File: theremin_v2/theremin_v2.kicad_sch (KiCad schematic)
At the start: 34 parts, among them J2 USB_C_Receptacle_USB2.0, J3 Conn_01x01_Pin, SW1 Reset, SW2 Boot, U1 AD8001AR, U2 HEF4093B, U3 AD8001AR, U4 ESP32-S2-SOLO, U5 LD1117S33TR_SOT223

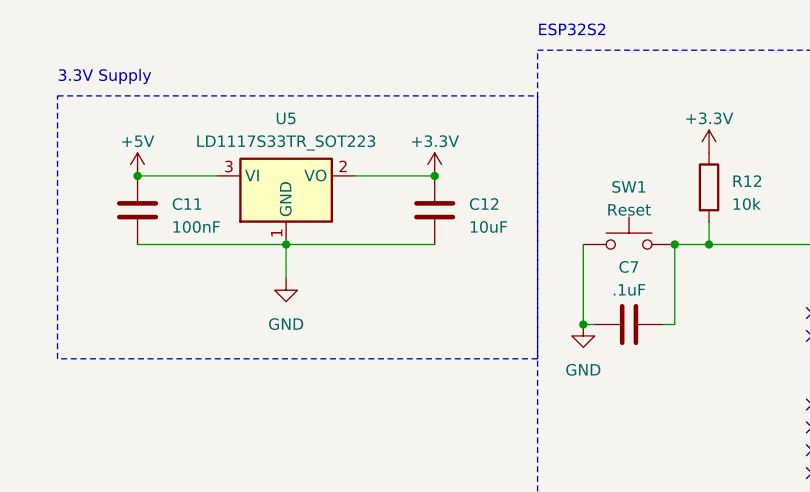
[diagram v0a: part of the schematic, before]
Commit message: BOM and some schematic updates
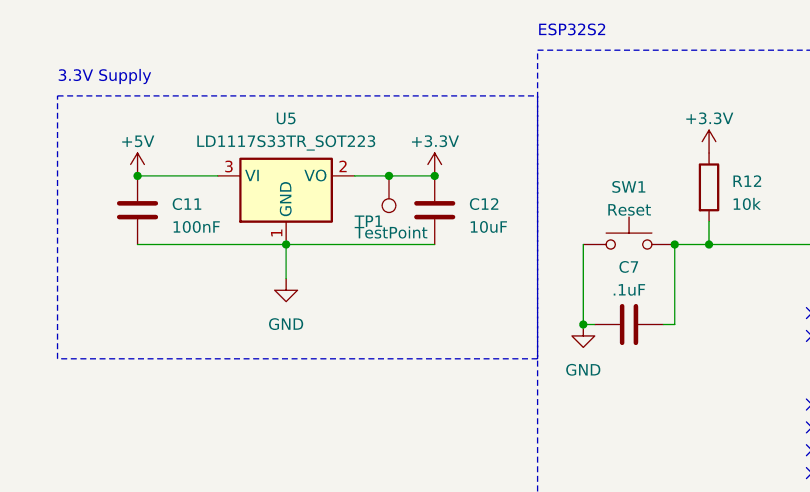
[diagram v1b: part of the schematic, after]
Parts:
- added TP1: TestPoint, TestPoint:TestPoint_THTPad_D2.0mm_Drill1.0mm, symbol Connector:TestPoint
- C10, C7, C9: footprint Capacitor_SMD:C_0201_0603Metric -> Capacitor_SMD:C_0402_1005Metric
- C12: footprint Capacitor_SMD:C_0201_0603Metric -> Capacitor_SMD:C_1206_3216Metric
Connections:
- net +3.3V: now also TP1.1
